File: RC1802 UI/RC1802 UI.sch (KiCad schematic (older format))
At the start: 47 parts, among them J1 Mount, J2 Mount, J3 Mount, J4 Mount, J6 CONN_02X20, SW1 RUN, SW10 IN5, SW11 IN6, SW12 IN7, SW2 IN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

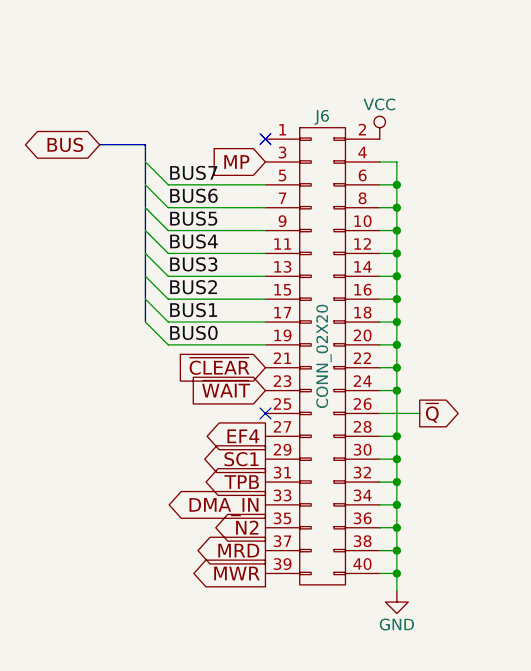
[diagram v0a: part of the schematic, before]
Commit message: UI PCB layout incorporating changes
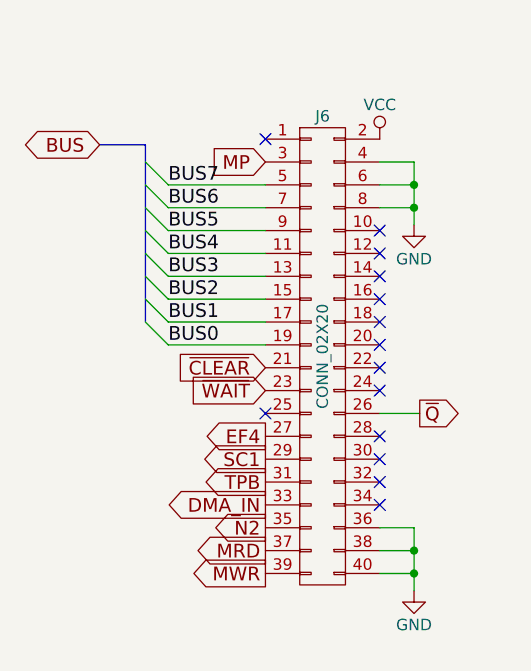
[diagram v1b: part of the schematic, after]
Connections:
- net GND: no longer J6.10 (P10), J6.12 (P12), J6.14 (P14), J6.16 (P16), J6.18 (P18), J6.20 (P20), J6.22 (P22), J6.24 (P24), J6.28 (P28), J6.30 (P30), J6.32 (P32), J6.34 (P34)
- no-connect marks 16 -> 28
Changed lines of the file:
@@
 L GND #PWR031
 U 1 1 594D8C76
-P 15450 9550
-F 0 "#PWR031" H 15450 9300 50  0001 C CNN
-F 1 "GND" H 15450 9400 50  0000 C CNN
-F 2 "" H 15450 9550 50  0001 C CNN
-F 3 "" H 15450 9550 50  0001 C CNN
-	1    15450 9550
+P 15525 9550
+F 0 "#PWR031" H 15525 9300 50  0001 C CNN
+F 1 "GND" H 15525 9400 50  0000 C CNN
+F 2 "" H 15525 9550 50  0001 C CNN
+F 3 "" H 15525 9550 50  0001 C CNN
+	1    15525 9550
 	1    0    0    -1
 $EndComp
@@
 MP
 NoConn ~ 14875 7575
-Wire Wire Line
-	15450 7675 15450 9550
-Wire Wire Line
-	15450 7675 15375 7675
-Wire Wire Line
-	15375 7775 15450 7775
-Connection ~ 15450 7775
-Wire Wire Line
-	15375 7875 15450 7875
-Connection ~ 15450 7875
-Wire Wire Line
-	15375 7975 15450 7975
-Connection ~ 15450 7975
-Wire Wire Line
-	15375 8075 15450 8075
-Connection ~ 15450 8075
-Wire Wire Line
-	15375 8175 15450 8175
-Connection ~ 15450 8175
-Wire Wire Line
-	15375 8275 15450 8275
-Connection ~ 15450 8275
-Wire Wire Line
-	15375 8375 15450 8375
-Connection ~ 15450 8375
-Wire Wire Line
-	15375 8475 15450 8475
-Connection ~ 15450 8475
-Wire Wire Line
-	15375 8575 15450 8575
-Connection ~ 15450 8575
-Wire Wire Line
-	15450 8675 15375 8675
-Connection ~ 15450 8675
-Wire Wire Line
-	15375 8875 15450 8875
-Connection ~ 15450 8875
-Wire Wire Line
-	15375 8975 15450 8975
-Connection ~ 15450 8975
-Wire Wire Line
-	15375 9075 15450 9075
-Connection ~ 15450 9075
-Wire Wire Line
-	15375 9175 15450 9175
-Connection ~ 15450 9175
-Wire Wire Line
-	15375 9275 15450 9275
-Connection ~ 15450 9275
-Wire Wire Line
-	15375 9375 15450 9375
-Connection ~ 15450 9375
-Wire Wire Line
-	15375 9475 15450 9475
-Connection ~ 15450 9475
 $Comp
 L VSS #PWR032
@@
 $EndComp
 NoConn ~ 14875 8775
+Wire Wire Line
+	15525 9275 15525 9550
+Wire Wire Line
+	15375 9275 15525 9275
+Wire Wire Line
+	15375 9375 15525 9375
+Connection ~ 15525 9375
+Wire Wire Line
+	15375 9475 15525 9475
+Connection ~ 15525 9475
+$Comp
+L GND #PWR034
+U 1 1 5BA7C55D
+P 15525 7950
+F 0 "#PWR034" H 15525 7700 50  0001 C CNN
+F 1 "GND" H 15525 7800 50  0000 C CNN
+F 2 "" H 15525 7950 50  0001 C CNN
+F 3 "" H 15525 7950 50  0001 C CNN
+	1    15525 7950
+	1    0    0    -1
+$EndComp
+Wire Wire Line
+	15525 7675 15525 7950
+Wire Wire Line
+	15375 7675 15525 7675
+Wire Wire Line
+	15375 7775 15525 7775
+Connection ~ 15525 7775
+Wire Wire Line
+	15375 7875 15525 7875
+Connection ~ 15525 7875
+NoConn ~ 15375 7975
+NoConn ~ 15375 8075
+NoConn ~ 15375 8175
+NoConn ~ 15375 8275
+NoConn ~ 15375 8375
+NoConn ~ 15375 8475
+NoConn ~ 15375 8575
+NoConn ~ 15375 8675
+NoConn ~ 15375 8875
+NoConn ~ 15375 8975
+NoConn ~ 15375 9075
+NoConn ~ 15375 9175
 $EndSCHEMATC

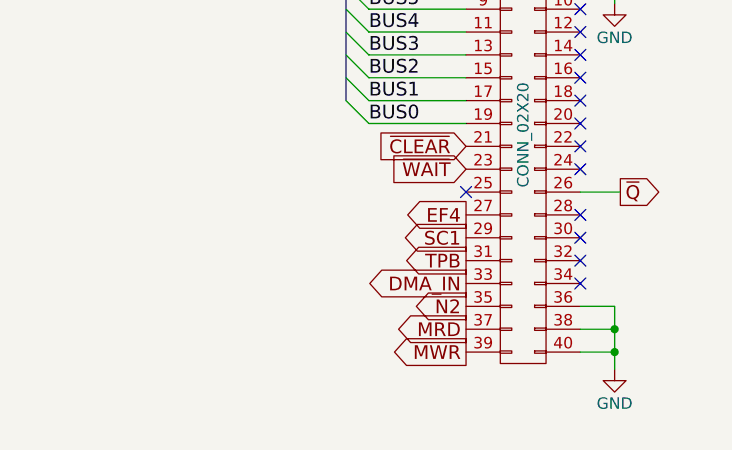
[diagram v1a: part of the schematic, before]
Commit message: Gerber export UI board
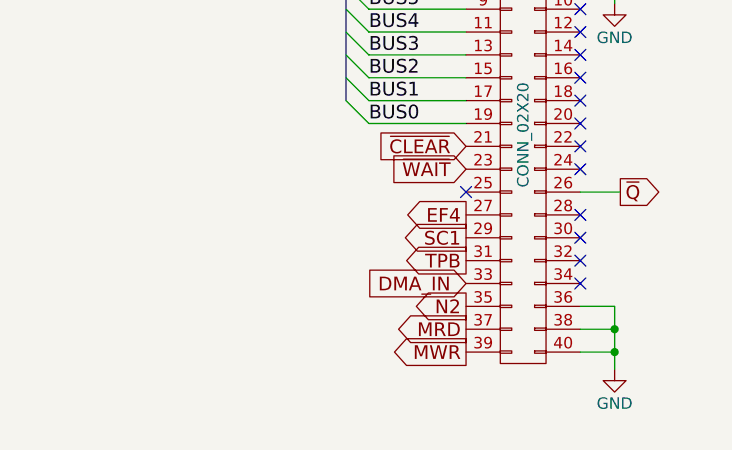
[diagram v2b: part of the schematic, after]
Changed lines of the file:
@@
 Text GLabel 14875 9275 0    60   Output ~ 0
 N2
-Text GLabel 14875 9175 0    60   Output ~ 0
+Text GLabel 14875 9175 0    60   Input ~ 0
 DMA_IN
 $Comp

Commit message: Changed UI connector
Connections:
- net GND: no longer J6.40 (P40), J6.8 (P8)
- net VCC: now also J6.40 (P40)
- no-connect marks 28 -> 29
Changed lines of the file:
@@
 	15375 9275 15525 9275
 Wire Wire Line
-	15375 9375 15525 9375
+	15525 9375 15375 9375
 Connection ~ 15525 9375
-Wire Wire Line
-	15375 9475 15525 9475
-Connection ~ 15525 9475
 $Comp
 L GND #PWR034
@@
 	15375 7675 15525 7675
 Wire Wire Line
-	15375 7775 15525 7775
+	15525 7775 15375 7775
 Connection ~ 15525 7775
-Wire Wire Line
-	15375 7875 15525 7875
-Connection ~ 15525 7875
 NoConn ~ 15375 7975
 NoConn ~ 15375 8075
@@
 NoConn ~ 15375 9075
 NoConn ~ 15375 9175
+NoConn ~ 15375 7875
+$Comp
+L VCC #PWR?
+U 1 1 5BC752AD
+P 15650 9475
+F 0 "#PWR?" H 15650 9325 50  0001 C CNN
+F 1 "VCC" H 15650 9625 50  0000 C CNN
+F 2 "" H 15650 9475 50  0001 C CNN
+F 3 "" H 15650 9475 50  0001 C CNN
+	1    15650 9475
+	1    0    0    -1
+$EndComp
+Wire Wire Line
+	15650 9475 15375 9475
 $EndSCHEMATC

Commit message: KiCad 5 update, both boards now marked F to match (without any actual changes)
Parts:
- AFF1, AFF2: symbol LTS-6980HR -> display:LTS-6980HR
- C1, C2, C3, C4, C5, C6, C7: symbol C_Small -> Device:C_Small
- D1: symbol LED -> Device:LED
- D2, D3, D4, D5, D6, D7: symbol D -> Device:D
- J1, J2, J3, J4: symbol CONN_01X01 -> RC1802-UI-rescue:CONN_01X01
- J6: symbol CONN_02X20 -> RC1802-UI-rescue:CONN_02X20
- JP1, JP2: symbol Jumper_NC_Small -> Device:Jumper_NC_Small
- R1, R2, R3, R4, R5: symbol R -> Device:R
- SW1, SW3, SW4: symbol SW_SPDT -> switches:SW_SPDT
- SW10, SW11, SW12, SW5, SW6, SW7, SW8, SW9: symbol SW_Push_SPDT -> switches:SW_Push_SPDT
- SW2: symbol NO/NC_Switch -> RC1802-UI-rescue:NO_NC_Switch
- U1: symbol 74LS04 -> RC1802-UI-rescue:74LS04
- U2: symbol 4050 -> cmos4000:4050
- U3: symbol 4013 -> cdp1802:4013
- U4: symbol 74LS10 -> RC1802-UI-rescue:74LS10
- U5, U7: symbol MC14495P1 -> cdp1802:MC14495P1
- U6: symbol 74LS244 -> RC1802-UI-rescue:74LS244
